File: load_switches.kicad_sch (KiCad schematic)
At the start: 12 parts

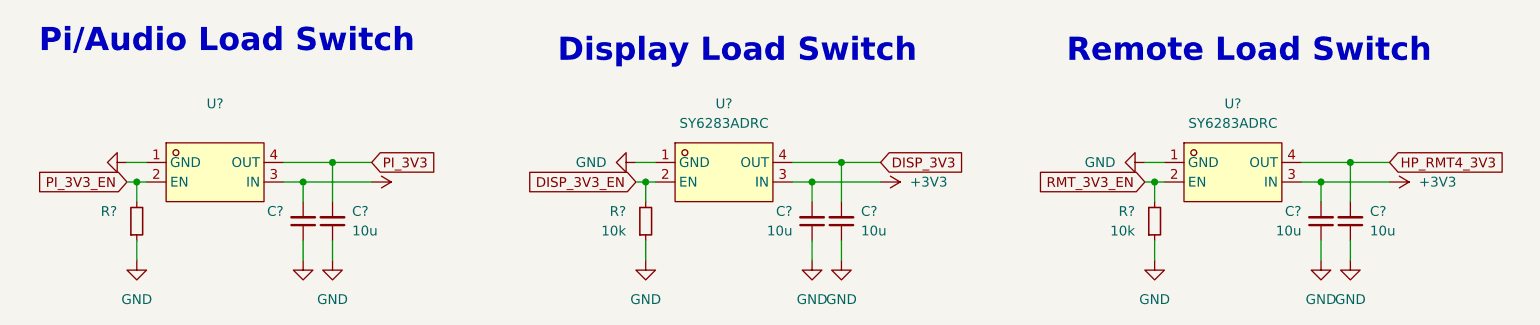
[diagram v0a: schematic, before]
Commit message: schem: first pass done, ERC passing
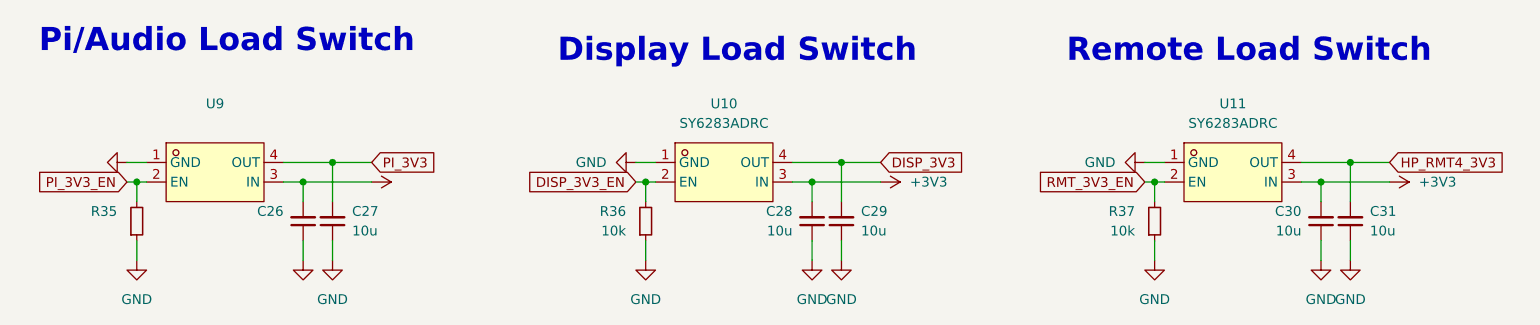
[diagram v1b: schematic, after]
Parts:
- U9: renamed from U?; footprint (none) -> lcsc:DFN-4_L1.6-W1.2-P0.50-BL
- gave numbers to parts that had none: 11
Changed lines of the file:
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@@
   (symbol (lib_id "power:GND") (at 160.02 95.25 0) (unit 1)
     (in_bom yes) (on_board yes) (fields_autoplaced)
-    (property "Reference" "#PWR?" (id 0) (at 160.02 101.6 0)
+    (property "Reference" "#PWR086" (id 0) (at 160.02 101.6 0)
       (effects (font (size 1.27 1.27)) hide)
     )
@@
   (symbol (lib_id "power:GND") (at 67.31 82.55 270) (unit 1)
     (in_bom yes) (on_board yes) (fields_autoplaced)
-    (property "Reference" "#PWR?" (id 0) (at 60.96 82.55 0)
+    (property "Reference" "#PWR078" (id 0) (at 60.96 82.55 0)
       (effects (font (size 1.27 1.27)) hide)
     )
@@
   (symbol (lib_id "power:GND") (at 156.21 95.25 0) (unit 1)
     (in_bom yes) (on_board yes) (fields_autoplaced)
-    (property "Reference" "#PWR?" (id 0) (at 156.21 101.6 0)
+    (property "Reference" "#PWR085" (id 0) (at 156.21 101.6 0)
       (effects (font (size 1.27 1.27)) hide)
     )
@@
   (symbol (lib_id "power:+3V3") (at 231.14 85.09 270) (unit 1)
     (in_bom yes) (on_board yes) (fields_autoplaced)
-    (property "Reference" "#PWR?" (id 0) (at 227.33 85.09 0)
+    (property "Reference" "#PWR092" (id 0) (at 227.33 85.09 0)
       (effects (font (size 1.27 1.27)) hide)
     )
@@
   (symbol (lib_id "power:+3V3") (at 165.1 85.09 270) (unit 1)
     (in_bom yes) (on_board yes) (fields_autoplaced)
-    (property "Reference" "#PWR?" (id 0) (at 161.29 85.09 0)
+    (property "Reference" "#PWR087" (id 0) (at 161.29 85.09 0)
       (effects (font (size 1.27 1.27)) hide)
     )
@@
   (symbol (lib_id "power:+3V3") (at 99.06 85.09 270) (unit 1)
     (in_bom yes) (on_board yes) (fields_autoplaced)
-    (property "Reference" "#PWR?" (id 0) (at 95.25 85.09 0)
+    (property "Reference" "#PWR082" (id 0) (at 95.25 85.09 0)
       (effects (font (size 1.27 1.27)) hide)
     )
@@
   (symbol (lib_id "power:GND") (at 133.35 82.55 270) (unit 1)
     (in_bom yes) (on_board yes) (fields_autoplaced)
-    (property "Reference" "#PWR?" (id 0) (at 127 82.55 0)
+    (property "Reference" "#PWR083" (id 0) (at 127 82.55 0)
       (effects (font (size 1.27 1.27)) hide)
     )
@@
   (symbol (lib_id "power:GND") (at 199.39 82.55 270) (unit 1)
     (in_bom yes) (on_board yes) (fields_autoplaced)
-    (property "Reference" "#PWR?" (id 0) (at 193.04 82.55 0)
+    (property "Reference" "#PWR088" (id 0) (at 193.04 82.55 0)
       (effects (font (size 1.27 1.27)) hide)
     )
@@
   (symbol (lib_id "lcsc:SY6283ADRC") (at 144.78 83.82 0) (unit 1)
     (in_bom yes) (on_board yes) (fields_autoplaced)
-    (property "Reference" "U?" (id 0) (at 144.78 74.93 0))
+    (property "Reference" "U10" (id 0) (at 144.78 74.93 0))
     (property "Value" "SY6283ADRC" (id 1) (at 144.78 77.47 0))
     (property "Footprint" "lcsc:DFN-4_L1.6-W1.2-P0.50-BL" (id 2) (at 144.78 92.71 0)
@@
   (symbol (lib_id "Device:C_Small") (at 160.02 90.17 180) (unit 1)
     (in_bom yes) (on_board yes) (fields_autoplaced)
-    (property "Reference" "C?" (id 0) (at 162.56 88.8935 0)
+    (property "Reference" "C29" (id 0) (at 162.56 88.8935 0)
       (effects (font (size 1.27 1.27)) (justify right))
     )
@@
   (symbol (lib_id "power:GND") (at 134.62 95.25 0) (unit 1)
     (in_bom yes) (on_board yes) (fields_autoplaced)
-    (property "Reference" "#PWR?" (id 0) (at 134.62 101.6 0)
+    (property "Reference" "#PWR084" (id 0) (at 134.62 101.6 0)
       (effects (font (size 1.27 1.27)) hide)
     )
@@
   (symbol (lib_id "Device:C_Small") (at 93.98 90.17 180) (unit 1)
     (in_bom yes) (on_board yes) (fields_autoplaced)
-    (property "Reference" "C?" (id 0) (at 96.52 88.8935 0)
+    (property "Reference" "C27" (id 0) (at 96.52 88.8935 0)
       (effects (font (size 1.27 1.27)) (justify right))
     )
@@
   (symbol (lib_id "Device:R_Small") (at 200.66 90.17 0) (mirror x) (unit 1)
     (in_bom yes) (on_board yes) (fields_autoplaced)
-    (property "Reference" "R?" (id 0) (at 198.12 88.8999 0)
+    (property "Reference" "R37" (id 0) (at 198.12 88.8999 0)
       (effects (font (size 1.27 1.27)) (justify right))
     )
@@
   (symbol (lib_id "Device:R_Small") (at 134.62 90.17 0) (mirror x) (unit 1)
     (in_bom yes) (on_board yes) (fields_autoplaced)
-    (property "Reference" "R?" (id 0) (at 132.08 88.8999 0)
+    (property "Reference" "R36" (id 0) (at 132.08 88.8999 0)
       (effects (font (size 1.27 1.27)) (justify right))
     )
@@
   (symbol (lib_id "lcsc:SY6283ADRC") (at 210.82 83.82 0) (unit 1)
     (in_bom yes) (on_board yes) (fields_autoplaced)
-    (property "Reference" "U?" (id 0) (at 210.82 74.93 0))
+    (property "Reference" "U11" (id 0) (at 210.82 74.93 0))
     (property "Value" "SY6283ADRC" (id 1) (at 210.82 77.47 0))
     (property "Footprint" "lcsc:DFN-4_L1.6-W1.2-P0.50-BL" (id 2) (at 210.82 92.71 0)
@@
   (symbol (lib_id "Device:R_Small") (at 68.58 90.17 0) (mirror x) (unit 1)
     (in_bom yes) (on_board yes) (fields_autoplaced)
-    (property "Reference" "R?" (id 0) (at 66.04 88.8999 0)
+    (property "Reference" "R35" (id 0) (at 66.04 88.8999 0)
       (effects (font (size 1.27 1.27)) (justify right))
     )
@@
   (symbol (lib_id "Device:C_Small") (at 226.06 90.17 180) (unit 1)
     (in_bom yes) (on_board yes) (fields_autoplaced)
-    (property "Reference" "C?" (id 0) (at 228.6 88.8935 0)
+    (property "Reference" "C31" (id 0) (at 228.6 88.8935 0)
       (effects (font (size 1.27 1.27)) (justify right))
     )
@@
   (symbol (lib_id "Device:C_Small") (at 156.21 90.17 0) (mirror x) (unit 1)
     (in_bom yes) (on_board yes) (fields_autoplaced)
-    (property "Reference" "C?" (id 0) (at 153.67 88.8935 0)
+    (property "Reference" "C28" (id 0) (at 153.67 88.8935 0)
       (effects (font (size 1.27 1.27)) (justify right))
     )
@@
   (symbol (lib_id "power:GND") (at 200.66 95.25 0) (unit 1)
     (in_bom yes) (on_board yes) (fields_autoplaced)
-    (property "Reference" "#PWR?" (id 0) (at 200.66 101.6 0)
+    (property "Reference" "#PWR089" (id 0) (at 200.66 101.6 0)
       (effects (font (size 1.27 1.27)) hide)
     )
@@
   (symbol (lib_id "power:GND") (at 68.58 95.25 0) (unit 1)
     (in_bom yes) (on_board yes) (fields_autoplaced)
-    (property "Reference" "#PWR?" (id 0) (at 68.58 101.6 0)
+    (property "Reference" "#PWR079" (id 0) (at 68.58 101.6 0)
       (effects (font (size 1.27 1.27)) hide)
     )
@@
   (symbol (lib_id "power:GND") (at 90.17 95.25 0) (unit 1)
     (in_bom yes) (on_board yes) (fields_autoplaced)
-    (property "Reference" "#PWR?" (id 0) (at 90.17 101.6 0)
+    (property "Reference" "#PWR080" (id 0) (at 90.17 101.6 0)
       (effects (font (size 1.27 1.27)) hide)
     )
@@
   (symbol (lib_id "power:GND") (at 222.25 95.25 0) (unit 1)
     (in_bom yes) (on_board yes) (fields_autoplaced)
-    (property "Reference" "#PWR?" (id 0) (at 222.25 101.6 0)
+    (property "Reference" "#PWR090" (id 0) (at 222.25 101.6 0)
       (effects (font (size 1.27 1.27)) hide)
     )
@@
   (symbol (lib_id "lcsc:SY6283ADRC") (at 78.74 83.82 0) (unit 1)
     (in_bom yes) (on_board yes) (fields_autoplaced)
-    (property "Reference" "U?" (id 0) (at 78.74 74.93 0))
+    (property "Reference" "U9" (id 0) (at 78.74 74.93 0))
     (property "Value" "" (id 1) (at 78.74 77.47 0))
-    (property "Footprint" "" (id 2) (at 78.74 92.71 0)
+    (property "Footprint" "lcsc:DFN-4_L1.6-W1.2-P0.50-BL" (id 2) (at 78.74 92.71 0)
       (effects (font (size 1.27 1.27)) hide)
     )
@@
   (symbol (lib_id "Device:C_Small") (at 90.17 90.17 0) (mirror x) (unit 1)
     (in_bom yes) (on_board yes) (fields_autoplaced)
-    (property "Reference" "C?" (id 0) (at 87.63 88.8935 0)
+    (property "Reference" "C26" (id 0) (at 87.63 88.8935 0)
       (effects (font (size 1.27 1.27)) (justify right))
     )
@@
   (symbol (lib_id "power:GND") (at 226.06 95.25 0) (unit 1)
     (in_bom yes) (on_board yes) (fields_autoplaced)
-    (property "Reference" "#PWR?" (id 0) (at 226.06 101.6 0)
+    (property "Reference" "#PWR091" (id 0) (at 226.06 101.6 0)
       (effects (font (size 1.27 1.27)) hide)
     )
@@
   (symbol (lib_id "power:GND") (at 93.98 95.25 0) (unit 1)
     (in_bom yes) (on_board yes) (fields_autoplaced)
-    (property "Reference" "#PWR?" (id 0) (at 93.98 101.6 0)
+    (property "Reference" "#PWR081" (id 0) (at 93.98 101.6 0)
       (effects (font (size 1.27 1.27)) hide)
     )
@@
   (symbol (lib_id "Device:C_Small") (at 222.25 90.17 0) (mirror x) (unit 1)
     (in_bom yes) (on_board yes) (fields_autoplaced)
-    (property "Reference" "C?" (id 0) (at 219.71 88.8935 0)
-      (effects (font (size 1.27 1.27)) (justify right))
-    )
+    (property "Reference" "C30" (id 0) (at 219.71 88.8935 0)
+      (effects (font (size 1.27 1.27)) (justify right))
+    )

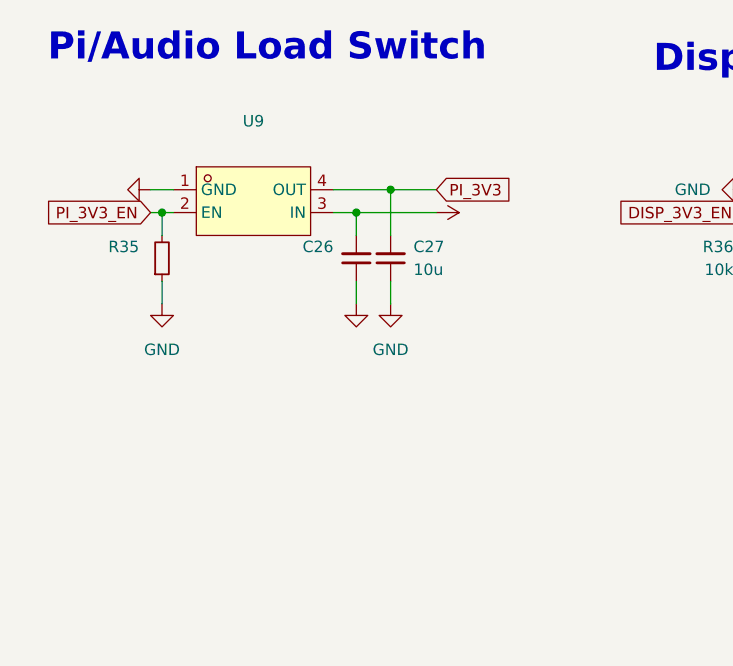
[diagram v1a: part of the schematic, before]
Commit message: analysis: specify pi will be powered directly from VCC
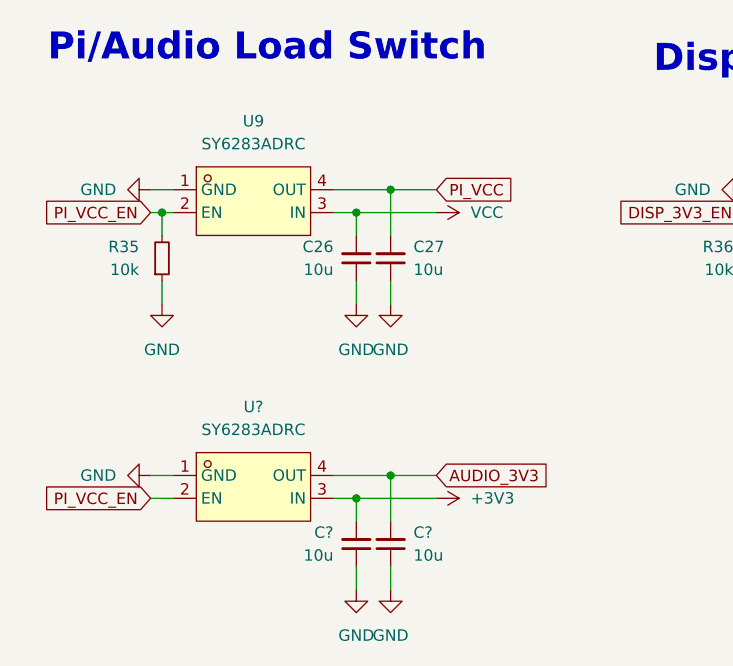
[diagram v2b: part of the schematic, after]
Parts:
- added C? (x2): 10u, Capacitor_SMD:C_0402_1005Metric, symbol Device:C_Small
- added U?: SY6283ADRC, lcsc:DFN-4_L1.6-W1.2-P0.50-BL, symbol lcsc:SY6283ADRC
- C26: value (none) -> 10u; footprint (none) -> Capacitor_SMD:C_0402_1005Metric
- C27, C28, C29, C30, C31: footprint (none) -> Capacitor_SMD:C_0402_1005Metric
- R35: value (none) -> 10k; footprint (none) -> Resistor_SMD:R_0402_1005Metric
- R36, R37: footprint (none) -> Resistor_SMD:R_0402_1005Metric
- U9: value (none) -> SY6283ADRC
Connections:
- net +3V3: now also C?.2, U?.3 (IN); no longer C26.2, U9.3 (IN)
- net GND: now also C?.1, C?.1, U?.1 (GND)
- net PI_3V3 renamed PI_VCC
- net PI_3V3_EN renamed PI_VCC_EN
- net PI_VCC_EN: now also U?.2 (EN)
- new net AUDIO_3V3: C?.2, U?.4 (OUT)
- new net VCC: C26.2, U9.3 (IN)

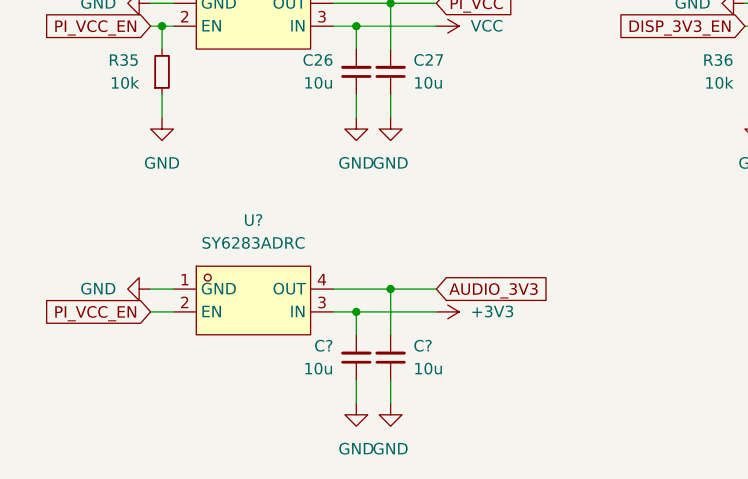
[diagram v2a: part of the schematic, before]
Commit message: analysis: change system regulator to one with lower dropout
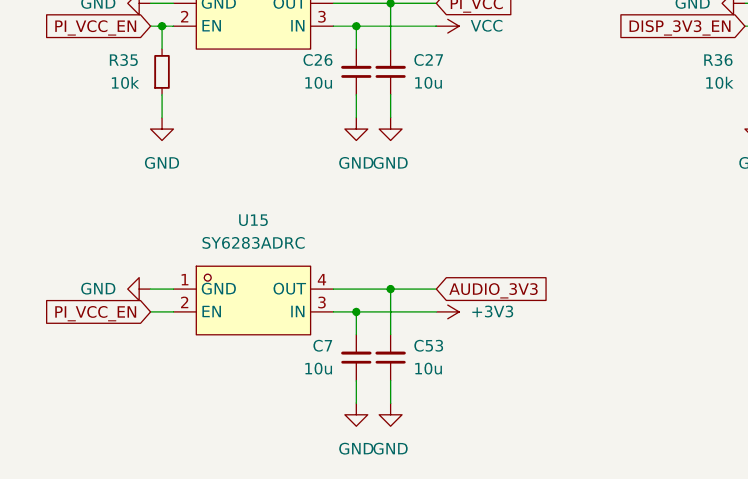
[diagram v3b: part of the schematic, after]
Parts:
- gave numbers to parts that had none: 3
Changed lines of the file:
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@@
   (symbol (lib_id "lcsc:SY6283ADRC") (at 78.74 115.57 0) (unit 1)
     (in_bom yes) (on_board yes) (fields_autoplaced)
-    (property "Reference" "U?" (id 0) (at 78.74 106.68 0))
+    (property "Reference" "U15" (id 0) (at 78.74 106.68 0))
     (property "Value" "SY6283ADRC" (id 1) (at 78.74 109.22 0))
     (property "Footprint" "lcsc:DFN-4_L1.6-W1.2-P0.50-BL" (id 2) (at 78.74 124.46 0)
@@
   (symbol (lib_id "Device:C_Small") (at 93.98 121.92 180) (unit 1)
     (in_bom yes) (on_board yes) (fields_autoplaced)
-    (property "Reference" "C?" (id 0) (at 96.52 120.6435 0)
+    (property "Reference" "C53" (id 0) (at 96.52 120.6435 0)
       (effects (font (size 1.27 1.27)) (justify right))
     )
@@
   (symbol (lib_id "Device:C_Small") (at 90.17 121.92 0) (mirror x) (unit 1)
     (in_bom yes) (on_board yes) (fields_autoplaced)
-    (property "Reference" "C?" (id 0) (at 87.63 120.6435 0)
+    (property "Reference" "C7" (id 0) (at 87.63 120.6435 0)
       (effects (font (size 1.27 1.27)) (justify right))
     )
@@
   (symbol (lib_id "power:GND") (at 90.17 127 0) (unit 1)
     (in_bom yes) (on_board yes) (fields_autoplaced)
-    (property "Reference" "#PWR?" (id 0) (at 90.17 133.35 0)
+    (property "Reference" "#PWR082" (id 0) (at 90.17 133.35 0)
       (effects (font (size 1.27 1.27)) hide)
     )
@@
   (symbol (lib_id "power:VCC") (at 99.06 85.09 270) (unit 1)
     (in_bom yes) (on_board yes) (fields_autoplaced)
-    (property "Reference" "#PWR?" (id 0) (at 95.25 85.09 0)
+    (property "Reference" "#PWR0124" (id 0) (at 95.25 85.09 0)
       (effects (font (size 1.27 1.27)) hide)
     )
@@
   (symbol (lib_id "power:GND") (at 93.98 127 0) (unit 1)
     (in_bom yes) (on_board yes) (fields_autoplaced)
-    (property "Reference" "#PWR?" (id 0) (at 93.98 133.35 0)
+    (property "Reference" "#PWR0123" (id 0) (at 93.98 133.35 0)
       (effects (font (size 1.27 1.27)) hide)
     )
@@
   (symbol (lib_id "power:+3V3") (at 99.06 116.84 270) (unit 1)
     (in_bom yes) (on_board yes) (fields_autoplaced)
-    (property "Reference" "#PWR?" (id 0) (at 95.25 116.84 0)
+    (property "Reference" "#PWR0125" (id 0) (at 95.25 116.84 0)
       (effects (font (size 1.27 1.27)) hide)
     )
@@
   (symbol (lib_id "power:GND") (at 67.31 114.3 270) (unit 1)
     (in_bom yes) (on_board yes) (fields_autoplaced)
-    (property "Reference" "#PWR?" (id 0) (at 60.96 114.3 0)
-      (effects (font (size 1.27 1.27)) hide)
-    )
+    (property "Reference" "#PWR033" (id 0) (at 60.96 114.3 0)
+      (effects (font (size 1.27 1.27)) hide)
+    )
